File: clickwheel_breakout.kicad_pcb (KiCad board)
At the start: 2 copper layers, 95 x 55 mm, 14 parts, among them J1 1-2328724-3, J2 1-2328724-3, J3 Conn_01x13, SW1 MENU, SW2 ▶ ||, SW3 |◀◀, SW4 ▶▶|, SW5 ENTER

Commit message: Flip passthrough connector, add button silkscreens
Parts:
- J2: moved to B.Cu
- moved REF** 0.25 mm to (157.5, 65.8)
- turned J2 to 90 degrees
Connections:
- J2 pad 1: GND -> VCC
- J2 pad 10: P1_3 -> PB_UP
- J2 pad 11: P1_1 -> PB_LEFT
- J2 pad 12: P1_0 -> PB_MID
- J2 pad 13: VCC -> GND
- J2 pad 2: PB_MID -> P1_0
- J2 pad 3: PB_LEFT -> P1_1
- J2 pad 4: PB_UP -> P1_3
- J2 pad 5: PB_RIGHT -> P1_5
- J2 pad 6: PB_DOWN -> P1_7
- J2 pad 8: P1_7 -> PB_DOWN
- J2 pad 9: P1_5 -> PB_RIGHT
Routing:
- net PB_LEFT: track 119.2 -> 131.0 mm
- net PB_RIGHT: track 150.8 -> 161.8 mm
- net P3_1: track 65.0 -> 75.0 mm
- net P1_5: track 71.0 -> 80.4 mm
- net P1_1: track 77.3 -> 85.4 mm
- net P1_0: track 62.7 -> 69.5 mm, vias 2 -> 1
- net P1_3: track 58.3 -> 62.4 mm, vias 2 -> 1
- net P1_7: track 53.8 -> 56.4 mm, vias 2 -> 1
- net VCC: track 5.94 -> 8.52 mm, vias 2 -> 1
- net PB_DOWN: track 131.2 -> 133.0 mm, vias 2 -> 1
- net PB_MID: track 113.0 -> 111.8 mm, vias 2 -> 1
- net GND: track 8.09 -> 8.73 mm, vias 0 -> 2
- net PB_UP: track 101.6 -> 102.1 mm, vias 3 -> 2
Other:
- board text added: "ENTER"
- board text added: "MB Passthrough"
- board text added: "MENU"
- board text added: "NEXT"
- board text added: "PLAY/PAUSE"
- board text added: "PREV"
- board text added: "iPod Clickwheel Breakout Rev 2"
- board text removed: "iPod Clickwheel Breakout Rev 1"

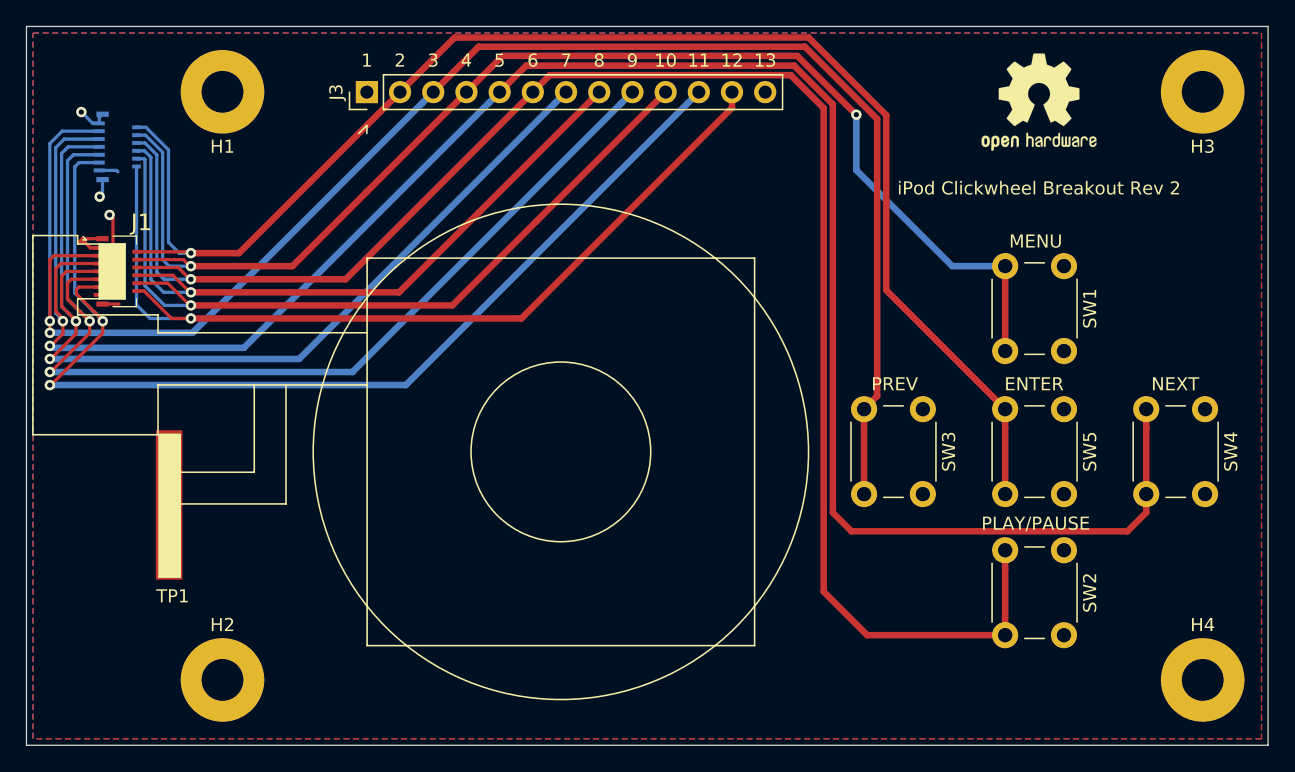
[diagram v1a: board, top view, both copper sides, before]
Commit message: Round PCB corners
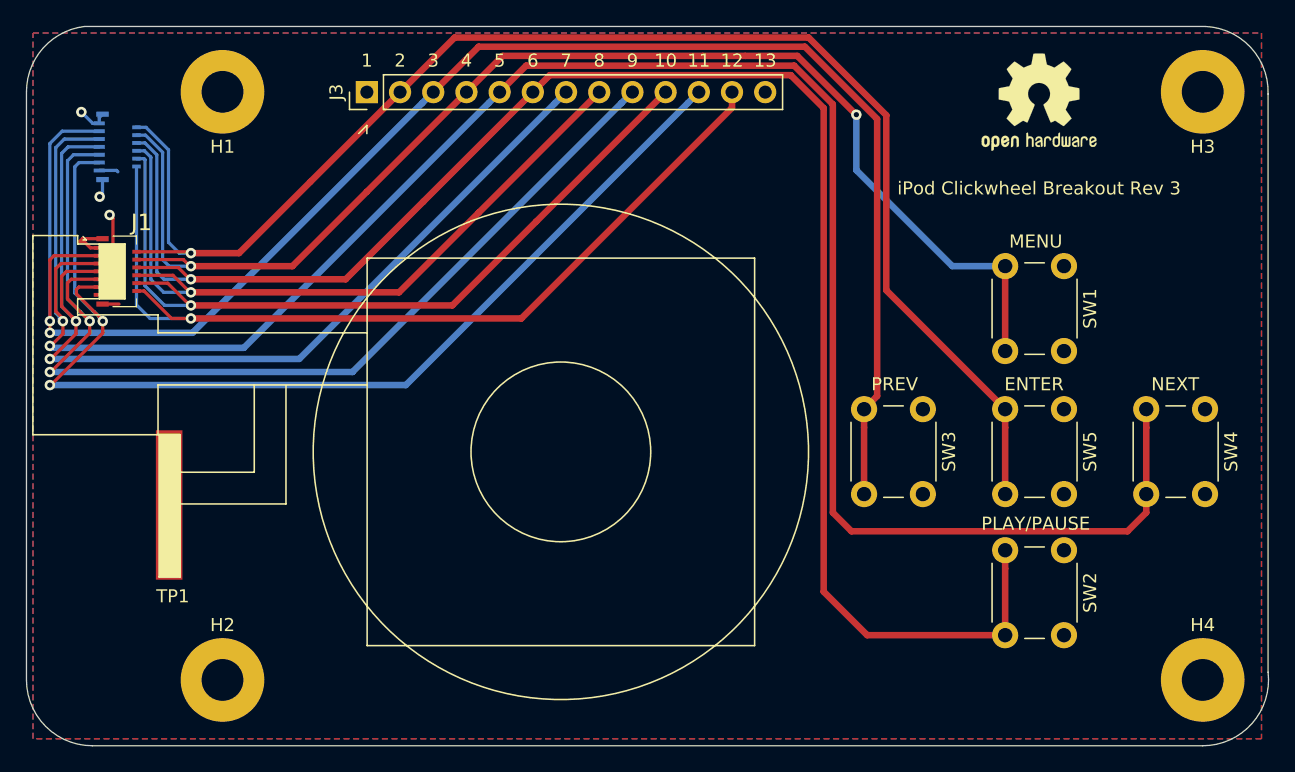
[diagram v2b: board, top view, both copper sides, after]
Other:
- outline, holes or cut-outs redrawn
- board text added: "iPod Clickwheel Breakout Rev 3"
- board text removed: "iPod Clickwheel Breakout Rev 2"
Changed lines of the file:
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@@
   (general
     (thickness 1.6)
-    (drawings 33)
+    (drawings 37)
     (tracks 228)
     (zones 0)
@@
       (outputformat 1)
       (mirror false)
-      (drillshape 1)
+      (drillshape 0)
       (scaleselection 1)
-      (outputdirectory ""))
+      (outputdirectory "../export/"))
   )
   (net 0 "")
@@
     (effects (font (size 0.8 0.6) (thickness 0.1)) (justify mirror))
   )
-  (gr_text "iPod Clickwheel Breakout Rev 2\n" (at 157.48 72.39) (layer F.SilkS)
+  (gr_text "iPod Clickwheel Breakout Rev 3" (at 157.48 72.39) (layer F.SilkS)
     (effects (font (size 1 1) (thickness 0.15)))
   )
@@
   (gr_line (start 106.045 67.564) (end 106.045 68.199) (layer F.SilkS) (width 0.12))
   (gr_line (start 105.41 68.199) (end 106.045 67.564) (layer F.SilkS) (width 0.12))
-  (gr_line (start 80 115) (end 80 60) (layer Edge.Cuts) (width 0.05))
-  (gr_line (start 175 115) (end 80 115) (layer Edge.Cuts) (width 0.05))
-  (gr_line (start 175 60) (end 175 115) (layer Edge.Cuts) (width 0.05))
-  (gr_line (start 80 60) (end 175 60) (layer Edge.Cuts) (width 0.05))
+  (gr_line (start 80 110) (end 80 65) (angle 90) (layer Edge.Cuts) (width 0.05))
+  (gr_line (start 170.001 115.036) (end 85.035 115.036) (angle 90) (layer Edge.Cuts) (width 0.05))
+  (gr_line (start 175.001 65.17) (end 175.001 109.411) (angle 90) (layer Edge.Cuts) (width 0.05))
+  (gr_line (start 84.437 60) (end 170.2 60) (angle 90) (layer Edge.Cuts) (width 0.05))
+  (gr_arc (start 170 65) (end 175.001 65.17) (angle -89.657) (layer Edge.Cuts) (width 0.05))
+  (gr_arc (start 170 110) (end 170.001 115.036) (angle -96.707) (layer Edge.Cuts) (width 0.05))
+  (gr_arc (start 85.036 65) (end 84.437 60) (angle -83.178) (layer Edge.Cuts) (width 0.05))
+  (gr_arc (start 85.036 110) (end 80 110) (angle -89.991) (layer Edge.Cuts) (width 0.05))
   (via (at 85.598 73.025) (size 0.8) (drill 0.4) (layers F.Cu B.Cu) (net 1))
   (segment (start 85.82 71.715) (end 85.82 72.803) (width 0.25) (layer B.Cu) (net 1))
@@
     (connect_pads (clearance 0.508))
     (min_thickness 0.254)
-    (fill yes (arc_segments 32) (thermal_gap 0.508) (thermal_bridge_width 0.508))
+    (fill yes (arc_segments 32) (thermal_gap 0.508) (thermal_bridge_width 0.508) (smoothing fillet) (radius 5))
     (polygon
       (pts
@@
     (connect_pads (clearance 0.508))
     (min_thickness 0.254)
-    (fill yes (arc_segments 32) (thermal_gap 0.508) (thermal_bridge_width 0.508))
+    (fill yes (arc_segments 32) (thermal_gap 0.508) (thermal_bridge_width 0.508) (smoothing fillet) (radius 5))
     (polygon
       (pts

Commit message: Switch to 2 row header to allow control of which lines are connected to mainboard
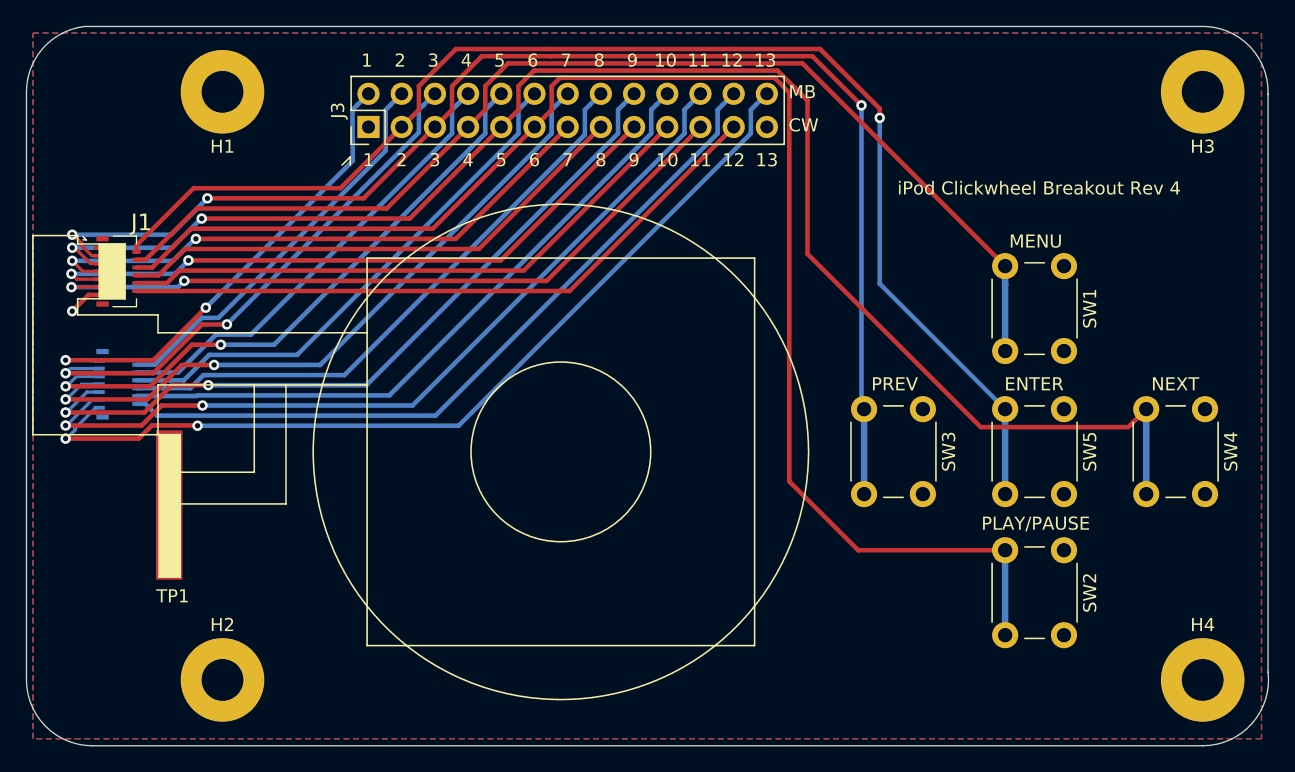
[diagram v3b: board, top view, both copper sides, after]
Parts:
- removed REF**: OSHW-Logo2_9.8x8mm_SilkScreen, Symbol:OSHW-Logo2_9.8x8mm_SilkScreen
- J3: value Conn_01x13 -> Conn_02x13_Odd_Even; footprint Connector_PinHeader_2.54mm:PinHeader_1x13_P2.54mm_Vertical -> Connector_PinHeader_2.54mm:PinHeader_2x13_P2.54mm_Vertical
- moved J2 18.2 mm to (87.0, 87.4)
- moved J3 2.67 mm to (106.2, 67.7)
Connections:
- J1 pad 10: P1_3 -> P1_3_CW
- J1 pad 11: P1_1 -> P1_1_CW
- J1 pad 12: P1_0 -> P1_0_CW
- J1 pad 2: PB_MID -> PB_MID_CW
- J1 pad 3: PB_LEFT -> PB_LEFT_CW
- J1 pad 4: PB_UP -> PB_UP_CW
- J1 pad 5: PB_RIGHT -> PB_RIGHT_CW
- J1 pad 6: PB_DOWN -> PB_DOWN_CW
- J1 pad 7: P3_1 -> P3_1_CW
- J1 pad 8: P1_7 -> P1_7_CW
- J1 pad 9: P1_5 -> P1_5_CW
- J1 pad MP1: GND -> Net-(J1-PadMP1)
- J1 pad MP2: GND -> Net-(J1-PadMP2)
- J2 pad 1: VCC -> VCC_MB
- J2 pad 10: PB_UP -> PB_UP_MB
- J2 pad 11: PB_LEFT -> PB_LEFT_MB
- J2 pad 12: PB_MID -> PB_MID_MB
- J2 pad 13: GND -> GND_MB
- J2 pad 2: P1_0 -> P1_0_MB
- J2 pad 3: P1_1 -> P1_1_MB
- J2 pad 4: P1_3 -> P1_3_MB
- J2 pad 5: P1_5 -> P1_5_MB
- J2 pad 6: P1_7 -> P1_7_MB
- J2 pad 7: P3_1 -> P3_1_MB
- J2 pad 8: PB_DOWN -> PB_DOWN_MB
- J2 pad 9: PB_RIGHT -> PB_RIGHT_MB
- J2 pad MP1: GND -> Net-(J2-PadMP1)
- J2 pad MP2: GND -> Net-(J2-PadMP2)
- J3 pad 10: P1_3 -> PB_RIGHT_MB
- J3 pad 11: P1_1 -> PB_DOWN_CW
- J3 pad 12: P1_0 -> PB_DOWN_MB
- J3 pad 13: VCC -> P3_1_CW
- J3 pad 2: PB_MID -> GND_MB
- J3 pad 3: PB_LEFT -> PB_MID_CW
- J3 pad 4: PB_UP -> PB_MID_MB
- J3 pad 5: PB_RIGHT -> PB_LEFT_CW
- J3 pad 6: PB_DOWN -> PB_LEFT_MB
- J3 pad 7: P3_1 -> PB_UP_CW
- J3 pad 8: P1_7 -> PB_UP_MB
- J3 pad 9: P1_5 -> PB_RIGHT_CW
- SW1 pad 2: PB_UP -> PB_UP_CW
- SW2 pad 2: PB_DOWN -> PB_DOWN_CW
- SW3 pad 2: PB_LEFT -> PB_LEFT_CW
- SW4 pad 2: PB_RIGHT -> PB_RIGHT_CW
- SW5 pad 2: PB_MID -> PB_MID_CW
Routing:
- net PB_RIGHT: track 161.8 -> 0.00 mm, vias 2 -> 0
- net PB_DOWN: track 133.0 -> 0.00 mm, vias 1 -> 0
- net PB_LEFT: track 131.0 -> 0.00 mm, vias 2 -> 0
- net PB_RIGHT_CW: track 0.00 -> 116.7 mm, vias 0 -> 2
- net PB_DOWN_CW: track 0.00 -> 112.4 mm
- net PB_MID: track 111.8 -> 0.00 mm, vias 1 -> 0
- net PB_UP: track 102.1 -> 0.00 mm, vias 2 -> 0
- net PB_LEFT_CW: track 0.00 -> 101.3 mm, vias 0 -> 3
- net PB_MID_CW: track 0.00 -> 100.0 mm, vias 0 -> 1
- net PB_UP_CW: track 0.00 -> 86.7 mm
- net P1_1: track 85.4 -> 0.00 mm, vias 2 -> 0
- net P1_5: track 80.4 -> 0.00 mm, vias 2 -> 0
- net P3_1: track 75.0 -> 0.00 mm, vias 2 -> 0
- net P1_0: track 69.5 -> 0.00 mm, vias 1 -> 0
- net VCC_MB: track 0.00 -> 69.3 mm, vias 0 -> 2
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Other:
- board text added: "CW"
- board text added: "MB"
- board text added: "iPod Clickwheel Breakout Rev 4"
- board text removed: "iPod Clickwheel Breakout Rev 3"

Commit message: Add OSHW logo, update preview
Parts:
- added REF**: OSHW-Logo_5.7x6mm_SilkScreen, Symbol:OSHW-Logo_5.7x6mm_SilkScreen, F.Cu at (156.7, 66.9)
